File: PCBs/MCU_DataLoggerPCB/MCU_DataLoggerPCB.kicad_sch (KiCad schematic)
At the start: 25 parts, among them U1 24LC1025, U2 24LC1025, U3 DS1337S+, U4 ATMEGA328P-AU, Y1 32.768 kHz, Y2 16 MHz

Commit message: Project: completed comments
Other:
- note added: "EEPROM"
- note added: "MCU"
- note added: "Mounting"
- note added: "Real Time Clock"
- moved on the sheet: BT1, C1, C2, C3, C4, C5, D1, D2, H1, H2, H3, H4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

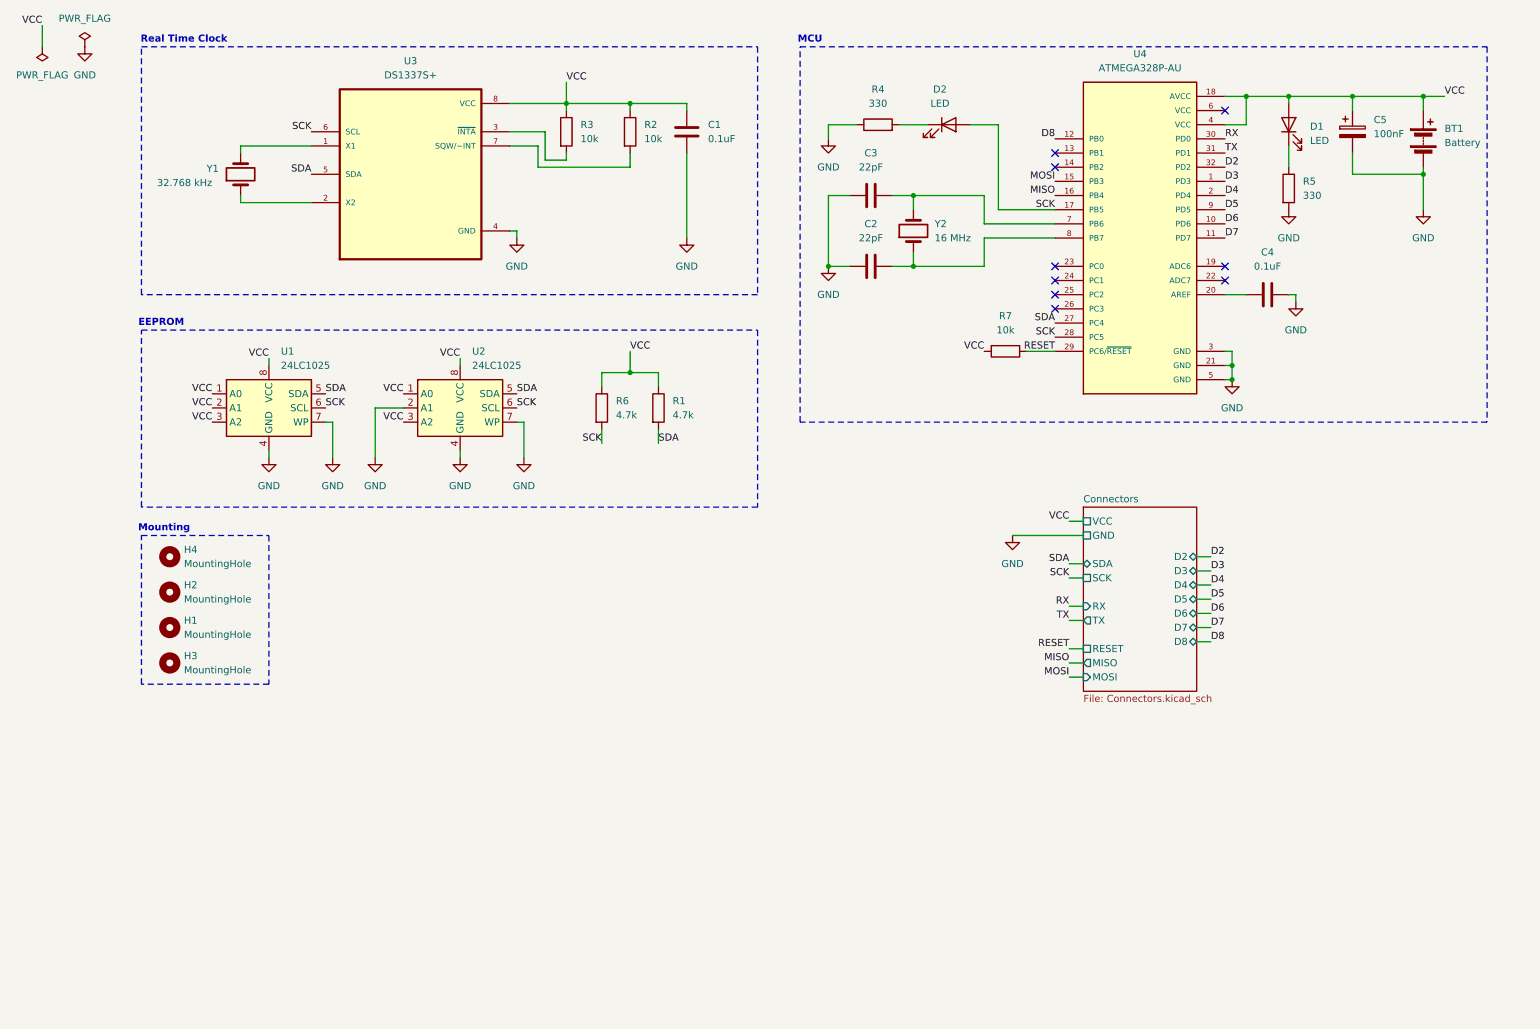
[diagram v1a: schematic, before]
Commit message: Project: Fix defect with SCK and SCL clocks in the schematic
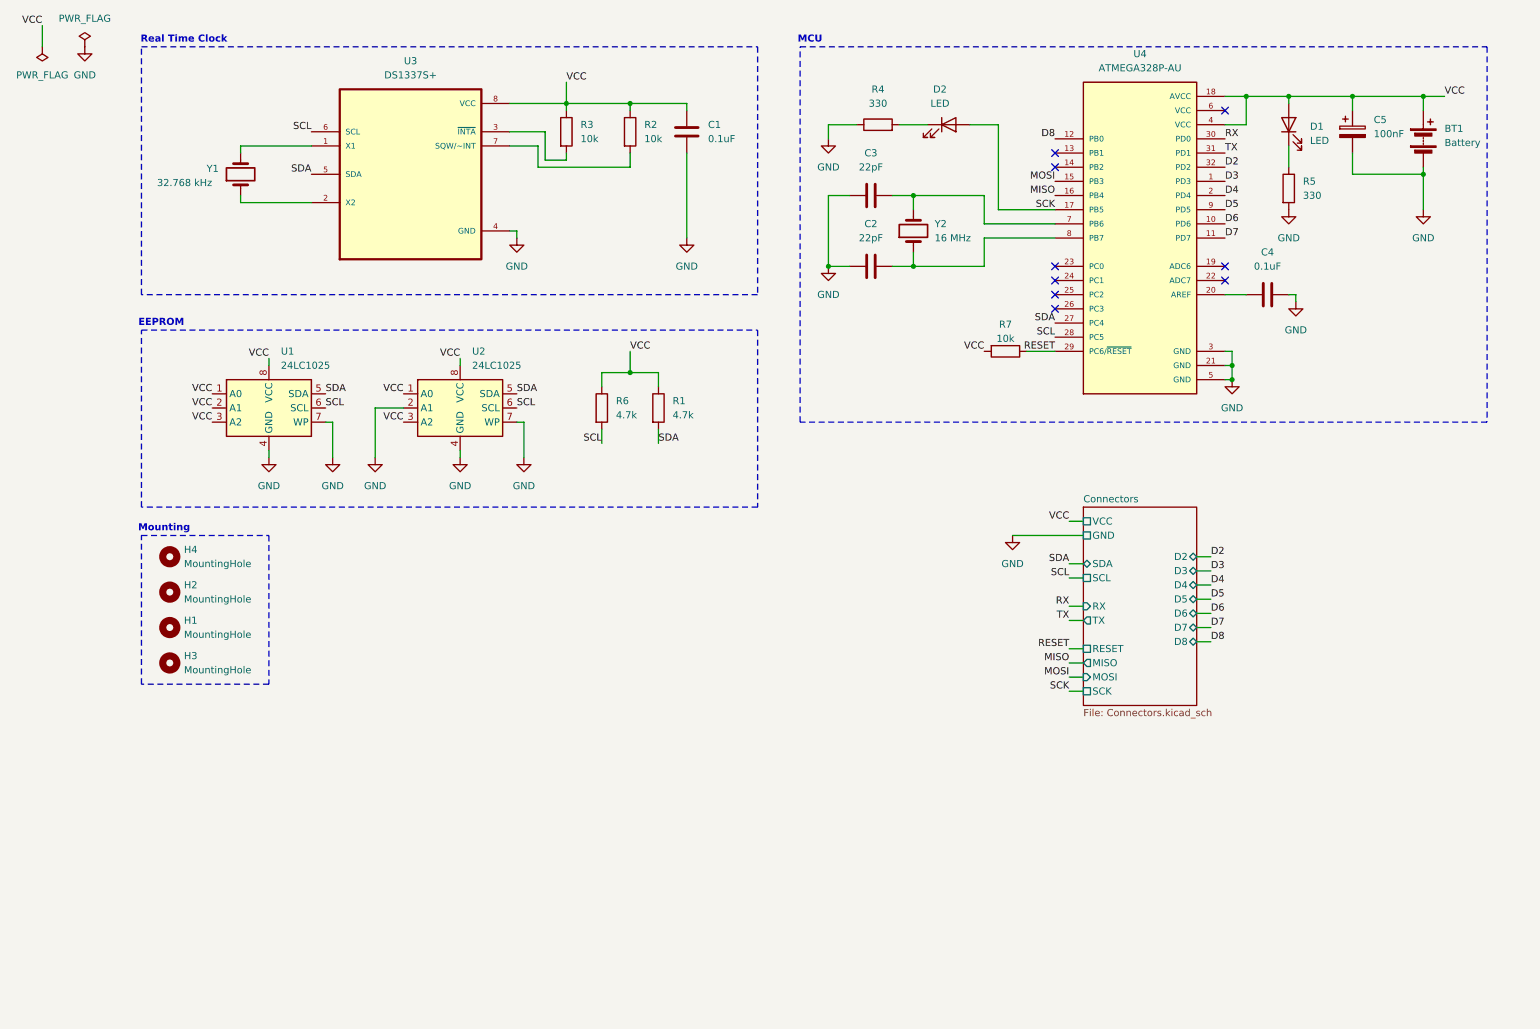
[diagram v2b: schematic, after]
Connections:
- net SCK: no longer R6.2, U1.6 (SCL), U2.6 (SCL), U3.6 (SCL), U4.28 (PC5)
- new net SCL: R6.2, U1.6 (SCL), U2.6 (SCL), U3.6 (SCL), U4.28 (PC5)
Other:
- sheet Connectors ports: added SCL; removed none
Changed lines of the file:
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@@
 	(wire
 		(pts
+			(xy 201.93 134.62) (xy 204.47 134.62)
+		)
+		(stroke
+			(width 0)
+			(type default)
+		)
+	)
+	(wire
+		(pts
 			(xy 106.68 36.83) (xy 101.6 36.83)
 		)
@@
 		)
 	)
+	(label "SCK"
+		(at 201.93 134.62 180)
+		(effects
+			(font
+				(size 1.27 1.27)
+			)
+			(justify right bottom)
+		)
+	)
 	(label "TX"
 		(at 229.87 38.1 0)
@@
 		)
 	)
+	(label "SCL"
+		(at 201.93 114.3 180)
+		(effects
+			(font
+				(size 1.27 1.27)
+			)
+			(justify right bottom)
+		)
+	)
 	(label "SDA"
 		(at 199.39 68.58 180)
@@
 		)
 	)
-	(label "D4"
-		(at 229.87 45.72 0)
+	(label "SCL"
+		(at 118.11 90.17 180)
 		(effects
 			(font
 				(size 1.27 1.27)
 			)
-			(justify left bottom)
+			(justify right bottom)
 		)
 	)
-	(label "D5"
-		(at 229.87 48.26 0)
+	(label "D4"
+		(at 229.87 45.72 0)
 		(effects
 			(font
@@
 		)
 	)
-	(label "SCK"
-		(at 68.58 83.82 0)
+	(label "D5"
+		(at 229.87 48.26 0)
 		(effects
 			(font
@@
 		)
 	)
-	(label "SCK"
+	(label "SCL"
 		(at 199.39 71.12 180)
 		(effects
@@
 		)
 	)
-	(label "SCK"
-		(at 102.87 83.82 0)
+	(label "SCL"
+		(at 66.04 34.29 180)
 		(effects
 			(font
 				(size 1.27 1.27)
 			)
-			(justify left bottom)
+			(justify right bottom)
 		)
 	)
@@
 		)
 	)
-	(label "SCK"
-		(at 118.11 90.17 180)
-		(effects
-			(font
-				(size 1.27 1.27)
-			)
-			(justify right bottom)
-		)
-	)
 	(label "VCC"
 		(at 48.26 83.82 180)
@@
 		)
 	)
-	(label "SCK"
-		(at 66.04 34.29 180)
-		(effects
-			(font
-				(size 1.27 1.27)
-			)
-			(justify right bottom)
-		)
-	)
 	(label "D7"
 		(at 229.87 53.34 0)
@@
 		)
 	)
+	(label "SCL"
+		(at 68.58 83.82 0)
+		(effects
+			(font
+				(size 1.27 1.27)
+			)
+			(justify left bottom)
+		)
+	)
 	(label "VCC"
 		(at 92.71 74.93 180)
@@
 		)
 	)
+	(label "SCL"
+		(at 102.87 83.82 0)
+		(effects
+			(font
+				(size 1.27 1.27)
+			)
+			(justify left bottom)
+		)
+	)
 	(label "D6"
 		(at 227.33 120.65 0)
@@
 		)
 	)
-	(label "SCK"
-		(at 201.93 114.3 180)
-		(effects
-			(font
-				(size 1.27 1.27)
-			)
-			(justify right bottom)
-		)
-	)
 	(label "MOSI"
 		(at 201.93 132.08 180)
@@
 		(on_board yes)
 		(dnp no)
-		(fields_autoplaced yes)
 		(property "Reference" "R7"
-			(at 190.5 67.31 90)
+			(at 190.5 68.834 90)
 			(effects
 				(font
@@
 		)
 		(property "Value" "10k"
-			(at 190.5 69.85 90)
+			(at 190.5 71.374 90)
 			(effects
 				(font
@@
 	(sheet
 		(at 204.47 101.6)
-		(size 20.32 33.02)
+		(size 20.32 35.56)
 		(exclude_from_sim no)
 		(in_bom yes)
@@
 		)
 		(property "Sheetfile" "Connectors.kicad_sch"
-			(at 204.47 135.2046 0)
+			(at 204.47 137.7446 0)
 			(effects
 				(font
@@
 			)
 		)
-		(pin "SCK" passive
-			(at 204.47 114.3 180)
-			(effects
-				(font
-					(size 1.27 1.27)
-				)
-				(justify left)
-			)
-		)
 		(pin "TX" output
 			(at 204.47 121.92 180)
@@
 			(effects
 				(font
+					(size 1.27 1.27)
+				)
+				(justify left)
+			)
+		)
+		(pin "SCK" passive
+			(at 204.47 134.62 180)
+			(effects
+				(font
+					(size 1.27 1.27)
+				)
+				(justify left)
+			)
+		)
+		(pin "SCL" passive
+			(at 204.47 114.3 180)
+			(effects
+				(font
